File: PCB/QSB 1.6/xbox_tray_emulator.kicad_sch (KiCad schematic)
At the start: 6 parts, among them J1 to Xbox, U1 ATtiny13A-S, U2 AP2127N-3.3

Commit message: add net lables, add firmware, update .gitignore
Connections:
- net GND: now reaches C1.2, C2.2, J1.11 (Pin_11), J1.12 (Pin_12), J1.3 (Pin_3), U1.4 (GND), U2.1 (GND)
- net 12V: now reaches J1.1 (Pin_1)
- net 12V: now also J1.9 (Pin_9)
- net NC: now reaches J1.13 (Pin_13)
- net NEJECT: now reaches J1.4 (Pin_4), U1.5 (PB0)
- net TRAY_OUT: now reaches J1.5 (Pin_5), U1.3 (PB4)
- net CD_RDY: now reaches J1.6 (Pin_6), U1.6 (PB1)
- net TRAY_IN: now reaches J1.7 (Pin_7), U1.2 (PB3)
- net SER_DATA: now reaches J1.8 (Pin_8), U1.7 (PB2)
- net RSET: now reaches R1.2, U1.1 (~{RESET}/PB5)
- net Net-(J1-Pad10) renamed 5V
- net Net-(R1-Pad1) renamed 3V3
- no-connect marks 0 -> 3
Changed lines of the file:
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@@
 		(color 0 0 0 0)
 	)
+	(no_connect
+		(at 175.26 142.24)
+	)
+	(no_connect
+		(at 175.26 127)
+	)
+	(no_connect
+		(at 175.26 132.08)
+	)
 	(wire
 		(pts
@@
 	(wire
 		(pts
+			(xy 171.45 142.24) (xy 175.26 142.24)
+		)
+		(stroke
+			(width 0)
+			(type default)
+		)
+	)
+	(wire
+		(pts
 			(xy 167.64 92.71) (xy 157.48 92.71)
 		)
@@
 	(wire
 		(pts
+			(xy 171.45 132.08) (xy 175.26 132.08)
+		)
+		(stroke
+			(width 0)
+			(type default)
+		)
+	)
+	(wire
+		(pts
 			(xy 144.78 132.08) (xy 143.51 132.08)
 		)
@@
 		)
 	)
-	(label "Net-(R1-Pad1)"
-		(at 154.94 74.93 180)
-		(effects
-			(font
-				(size 1.27 1.27)
-			)
-			(justify right bottom)
-		)
-	)
-	(label "Net-(J1-Pad10)"
-		(at 162.56 142.24 180)
-		(effects
-			(font
-				(size 1.27 1.27)
-			)
-			(justify right bottom)
-		)
-	)
+	(label "3V3"
+		(at 151.13 111.76 0)
+		(effects
+			(font
+				(size 1.27 1.27)
+			)
+			(justify left bottom)
+		)
+	)
+	(label "RSET"
+		(at 175.26 95.25 0)
+		(effects
+			(font
+				(size 1.27 1.27)
+			)
+			(justify left bottom)
+		)
+	)
+	(label "NC"
+		(at 175.26 127 0)
+		(effects
+			(font
+				(size 1.27 1.27)
+			)
+			(justify left bottom)
+		)
+	)
+	(label "12V"
+		(at 171.45 132.08 0)
+		(effects
+			(font
+				(size 1.27 1.27)
+			)
+			(justify left bottom)
+		)
+	)
+	(label "NEJECT"
+		(at 157.48 139.7 0)
+		(effects
+			(font
+				(size 1.27 1.27)
+			)
+			(justify left bottom)
+		)
+	)
+	(label "5V"
+		(at 151.13 140.97 0)
+		(effects
+			(font
+				(size 1.27 1.27)
+			)
+			(justify left bottom)
+		)
+	)
+	(label "TRAY_OUT"
+		(at 179.07 137.16 0)
+		(effects
+			(font
+				(size 1.27 1.27)
+			)
+			(justify left bottom)
+		)
+	)
+	(label "GND"
+		(at 162.56 124.46 0)
+		(effects
+			(font
+				(size 1.27 1.27)
+			)
+			(justify left bottom)
+		)
+	)
+	(label "SER_DATA"
+		(at 157.48 134.62 0)
+		(effects
+			(font
+				(size 1.27 1.27)
+			)
+			(justify left bottom)
+		)
+	)
+	(label "12V"
+		(at 171.45 142.24 0)
+		(effects
+			(font
+				(size 1.27 1.27)
+			)
+			(justify left bottom)
+		)
+	)
+	(label "TRAY_IN"
+		(at 179.07 134.62 0)
+		(effects
+			(font
+				(size 1.27 1.27)
+			)
+			(justify left bottom)
+		)
+	)
+	(label "CD_RDY"
+		(at 158.75 137.16 0)
+		(effects
+			(font
+				(size 1.27 1.27)
+			)
+			(justify left bottom)
+		)
+	)

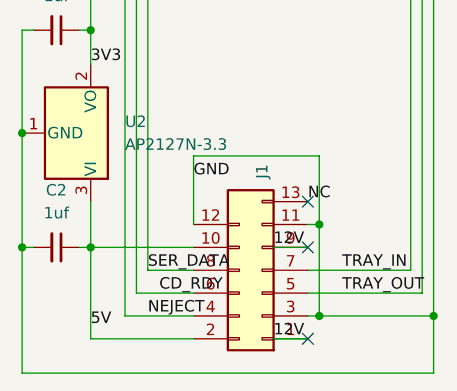
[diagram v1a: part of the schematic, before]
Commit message: adjust componets locations to make DRC happy, add gerbers.
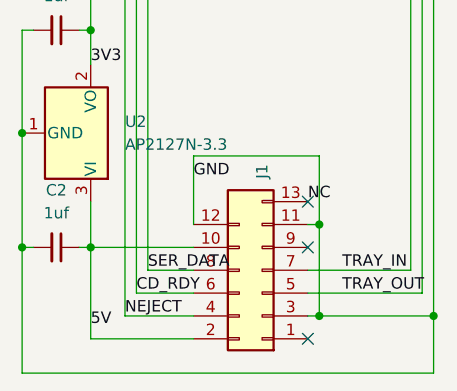
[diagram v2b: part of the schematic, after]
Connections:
- net 12V: no longer names the net of J1.1 (Pin_1)
- net 12V: no longer J1.9 (Pin_9)
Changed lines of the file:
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@@
+	)
+	(no_connect
+		(at 175.26 132.08)
+	)
+	(no_connect
+		(at 175.26 127)
 	)
 	(no_connect
 		(at 175.26 142.24)
 	)
-	(no_connect
-		(at 175.26 127)
-	)
-	(no_connect
-		(at 175.26 132.08)
-	)
 	(wire
 		(pts
@@
 	(wire
 		(pts
-			(xy 171.45 142.24) (xy 175.26 142.24)
-		)
-		(stroke
-			(width 0)
-			(type default)
-		)
-	)
-	(wire
-		(pts
 			(xy 167.64 92.71) (xy 157.48 92.71)
 		)
@@
 		(pts
 			(xy 154.94 90.17) (xy 154.94 139.7)
-		)
-		(stroke
-			(width 0)
-			(type default)
-		)
-	)
-	(wire
-		(pts
-			(xy 171.45 132.08) (xy 175.26 132.08)
 		)
 		(stroke
@@
 		)
 	)
-	(label "12V"
-		(at 171.45 132.08 0)
-		(effects
-			(font
-				(size 1.27 1.27)
-			)
-			(justify left bottom)
-		)
-	)
 	(label "NEJECT"
-		(at 157.48 139.7 0)
+		(at 154.94 139.7 0)
 		(effects
 			(font
@@
 		)
 	)
-	(label "12V"
-		(at 171.45 142.24 0)
-		(effects
-			(font
-				(size 1.27 1.27)
-			)
-			(justify left bottom)
-		)
-	)
 	(label "TRAY_IN"
 		(at 179.07 134.62 0)
@@
 	)
 	(label "CD_RDY"
-		(at 158.75 137.16 0)
-		(effects
-			(font
+		(at 156.21 137.16 0)
+		(effects
+			(font
